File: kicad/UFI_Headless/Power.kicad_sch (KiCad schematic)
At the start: 70 parts, among them J1 USB-C, J16 USB_HDR, J17 PSU_IN, J2 12V DC 5.5/2.1, J3 FDD_PWR, Q1 AO3401A, Q2 2N7002, Q3 AO3401A, Q4 2N7002, U1 USBLC6-2SC6, U12 INA180A1, U13 INA180A1, U19 TPS2116DRL, U2 TPS54202DDC, U24 USBLC6-2SC6, U3 TPS2116DRL, U4 AP7361C-33E

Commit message: KiCad v0.7 rework, stage A11c (owner's device-comparison list M2, order decided 2026-10-24: supply first): drive supplies through two TPS25921A eFuses - Power sheet: U28 (5 V) and U29 (12 V) TI TPS25921ADR (C189199, SOIC-8, JLC stock 681; new project symbol UFI_Headless:TPS25921A with the datasheet pinout 1 GND, 2 SS, 3 ENUV, 4 IN, 5 OUT, 6 FLT, 7 ILIM, 8 OVP) replace the polyfuses F2/F3 and the AO3401A/2N7002 switches Q1-Q4 with their gate network R27/R30/R32; R136/R142 150k (C22807) set the current limit to 1.43-1.7 A (datasheet table for R_ILIM = 150 k), OVP dividers R133/R134 33k/10k = 6.0 V and R138/R139/R140 100k/(10k+1k) = 14.0 V against the 1.39 V threshold (basic parts only, 91k/11k are extended), ENUV from FDD5_EN/FDD12_EN through R135/R141 10k while the existing 100k pull-downs R28/R31 keep both rails off in reset (ENUV threshold 1.39 V, 3.0 V applied), C81 2.2 nF (C1604) and C83 1 nF (C1588) give about 2.5 ms output ramp (datasheet: 1.2 nF = 3 ms at 11 V; measure at bring-up), C80/C82 100 nF at IN, FLT open drain with R137/R143 10k to +3V3 on the new global nets FLT5/FLT12; the shunts R26/R29 with U12/U13 INA180 stay behind the eFuse outputs (FDD5_F/FDD12_F -> shunt -> FDD_5V/FDD_12V, the old FDD5_S/FDD12_S nets are gone); D3 SMAJ15CA -> SMAJ13A (Diodes SMAJ13A-13-F C110519). MCU_Core: PF9 = FLT5, PF10 = FLT12 (no-connects removed). Old v0.2/v0.5 notes replaced by an A11c note. ERC over the whole project 0 errors / 0 warnings (build/erc.rpt). Firmware in the same commit: board.h/board_headless.c PIN_FLT5/PIN_FLT12 as inputs with pull-up (harmless on v0.x where the pins are open), ufi_board.c sample_faults() reads FLT only on board_rev >= 10 and only for a rail that is switched on (FLT is also low while ENUV is low), reports a change once as POWER event 0x83 with ERR LED and leaves the rail on because the eFuse retries by itself, board_status.power bits 2/3 carry the fault state; overcurrent comment updated (eFuse limit instead of polyfuse hold). Protocol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
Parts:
- removed F2, F3: 1.1A hold 24V, Fuse:Fuse_1812_4532Metric, symbol Device:Polyfuse
- removed Q1, Q3: AO3401A, Package_TO_SOT_SMD:SOT-23, symbol Transistor_FET:AO3401A
- removed Q2, Q4: 2N7002, Package_TO_SOT_SMD:SOT-23, symbol Transistor_FET:2N7002
- removed R27: 100k, Resistor_SMD:R_0603_1608Metric, symbol Device:R
- removed R30, R32: 10k, Resistor_SMD:R_0603_1608Metric, symbol Device:R
- added C80, C82: 100nF, Capacitor_SMD:C_0603_1608Metric, symbol Device:C
- added C81: 2.2nF, Capacitor_SMD:C_0603_1608Metric, symbol Device:C
- added C83: 1nF, Capacitor_SMD:C_0603_1608Metric, symbol Device:C
- added R133: 33k, Resistor_SMD:R_0603_1608Metric, symbol Device:R
- added R134, R135, R137, R139, R141, R143: 10k, Resistor_SMD:R_0603_1608Metric, symbol Device:R
- added R136, R142: 150k, Resistor_SMD:R_0603_1608Metric, symbol Device:R
- added R138: 100k, Resistor_SMD:R_0603_1608Metric, symbol Device:R
- added R140: 1k, Resistor_SMD:R_0603_1608Metric, symbol Device:R
- added U28, U29: TPS25921A, Package_SO:SOIC-8_3.9x4.9mm_P1.27mm, symbol UFI_Headless:TPS25921A
- D3: value SMAJ15CA -> SMAJ13A; LCSC C110044 -> C110519; MPN SMAJ15CA -> Diodes SMAJ13A-13-F (13 V standoff, 21.5 V clamp; A11c, was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
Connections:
- net FDD12_S is gone; now on net FDD_12V: R29.2, U13.4 (-)
- net FDD5_S is gone; now on net FDD_5V: R26.2, U12.4 (-)
- net +12V: now also C82.1, R138.1, U29.4 (IN)
- net +3V3: now also R137.1, R143.1
- net +5V: now also C80.1, R133.1, U28.4 (IN)
- net FDD12_EN: now also R141.1
- net FDD12_F: now also U29.5 (OUT)
- net FDD5_EN: now also R135.1
- net FDD5_F: now also U28.5 (OUT)
- net GND: now also C80.2, C81.2, C82.2, C83.2, R134.2, R136.2, R140.2, R142.2, U28.1 (GND), U29.1 (GND)
- new net ENUV12: R141.2, U29.3 (ENUV)
- new net ENUV5: R135.2, U28.3 (ENUV)
- new net FLT12: R143.2, U29.6 (FLT)
- new net FLT5: R137.2, U28.6 (FLT)
- new net ILIM12: R142.1, U29.7 (ILIM)
- new net ILIM5: R136.1, U28.7 (ILIM)
- new net OVP12: R138.2, R139.1, U29.8 (OVP)
- new net OVP12B: R139.2, R140.1
- new net OVP5: R133.2, R134.1, U28.8 (OVP)
- new net SS12: C83.1, U29.2 (SS)
- new net SS5: C81.1, U28.2 (SS)
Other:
- note added: "A11c (24.10.2026): drive supplies through TPS25921A eFuses U28 (5 V) / U29 (12 V) instead of the polyfuses F2/F3 and the AO3401A/2N7002 switches Q1-Q4. R_ILIM 150k -> current limit 1.43-1.7 A (datasheet table), fast trip and auto-retry; OVP divider 33k/10k = 6.0 V, 100k/(10k+1k) = 14.0 V (threshold 1.39 V); ENUV from FDD5_EN/FDD12_EN via 10k, the 100k pull-downs R28/R31 keep both rails off in res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"
- note removed: "v0.2: drive supplies (J3, Amiga J7) via polyfuses; test points TP1-TP4."
- note removed: "v0.5: FDD_5V / FDD_12V: polyfuse -> 0.1R shunt (INA180A1 -> I_FDD5/I_FDD12, 2 V/A) -> AO3401A high-side switch (FDD5_EN/FDD12_EN high = on, 100k pull-downs = off in reset) -> TVS. 12V gate divider 10k/10k keeps Vgs at -6 V (AO3401A max +-12 V)."

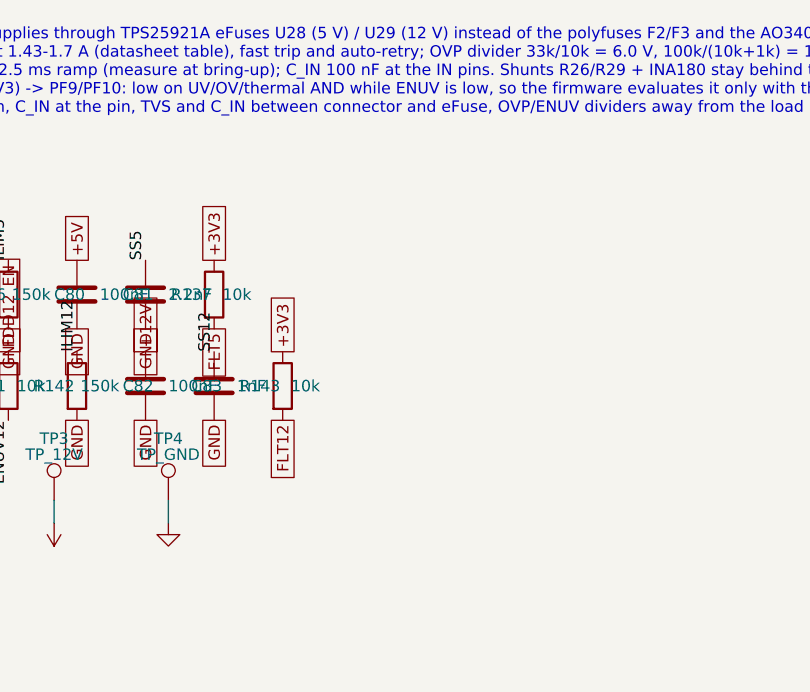
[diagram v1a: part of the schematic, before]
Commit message: KiCad v0.7 rework, stage A11d part 1 (owner's device-comparison list M5, S1-S4, S6; pins per docs/Timer_Zuteilung.md): sync sensor, J6 pin 2/4/33, rail voltage sense - Apple_Port: J19 pin 3 leaves the INDEX bus and becomes SYNC_5V with R165 10k to +3V3 and D30 PESD3V3L1BA, the new third Schmitt inverter U26 74LVC14AD (C133541, single-unit project symbol UFI_Headless:74LVC14_1U) turns it into SYNC -> PC6 (TIM8_CH1, AF3), also reads J6 pin 2 (FD_DENSITY) and pin 4 (FD_PIN4) back as FDD_PIN2_IN -> PD14 / FDD_PIN4_IN -> PD15 and reserves input 9 for the Mac !CSTOUT line of K1 (no-connect until A11d part 2), unused inputs on GND, C86 100 nF. FDD_Connectors: J6 pin 4 gets its own open-drain output Q12 BSS138DW (C154900, channel 1, gate FDD_PIN4 = PF14 with R158 100k, termination R159 1k to FDD_5V); J6 pin 33 moves from a fixed GND to the solder jumper JP7 (bridged to GND by default) whose third pad carries FLIPPY = PB5 through R156 2.2k with R157 2.2k to GND (2.2k instead of the planned 2.4k because 2.2k C4190 is already in the BOM). Power: R160/R161 10k/10k (FDD_5V / 2 -> V_FDD5 = PC4, ADC1 INP4) and R162/R163 33k/10k (FDD_12V / 4.3 -> V_FDD12 = PC5, ADC1 INP8). MCU_Core: no-connects on PC6, PD14, PD15, PF14, PB5, PC4, PC5, PB1 replaced by the global labels; PB0 (MAC_SEL) and PA8 (MAC_PWM) stay no-connect until the Mac header comes in part 2, PB1 = MAC_CSTOUT is already wired to U26. ERC over the whole project 0 errors / 0 warnings (build/erc.rpt). Firmware in the same commit: board.h/board_headless.c define PIN_SYNC, PIN_FDD_PIN2_IN, PIN_FDD_PIN4_IN, PIN_FDD_PIN4, PIN_FDD_PIN33, PIN_MAC_SEL, PIN_MAC_PWM, PIN_MAC_CSTOUT and ADC_CH_V_FDD5/V_FDD12 and initialise them as inputs or released (low) outputs; the TIM8 capture of SYNC, the rail-voltage limits (4.5 V / 10.8 V) and the protocol access follow in stage A10 (protocol doc: one hunk in the INDEX_SIM bullet - the sync sensor no longer drives the INDEX bus on v1.0, apple_sync has no effect there until A10). ARM build 0 wa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
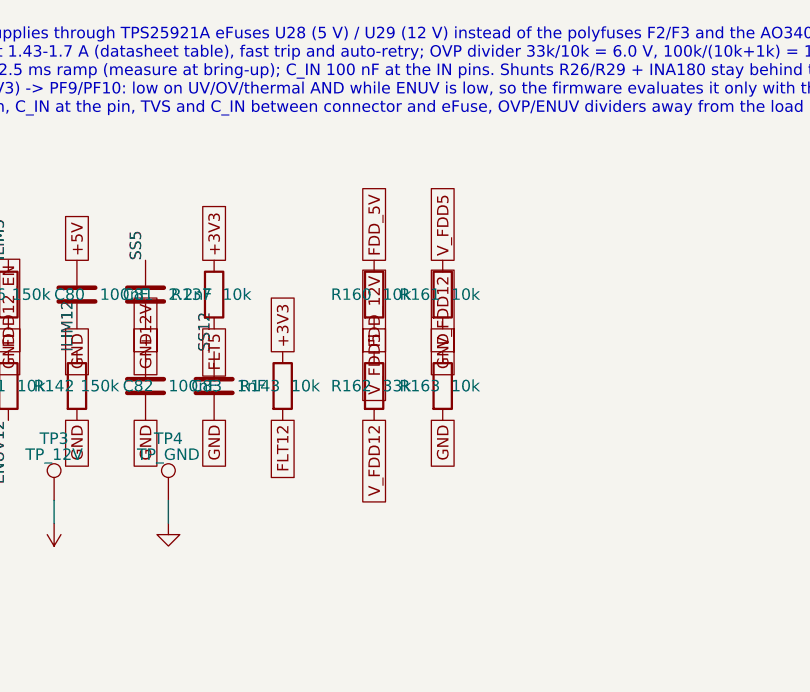
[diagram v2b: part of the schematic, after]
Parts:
- added R160, R161, R163: 10k, Resistor_SMD:R_0603_1608Metric, symbol Device:R
- added R162: 33k, Resistor_SMD:R_0603_1608Metric, symbol Device:R
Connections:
- net FDD_12V: now also R162.1
- net FDD_5V: now also R160.1
- net GND: now also R161.2, R163.2
- new net V_FDD12: R162.2, R163.1
- new net V_FDD5: R160.2, R161.1

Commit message: KiCad v0.7 rework, stage A11d part 2 (owner's list S5, S7, K1; owner decisions 2026-10-24: no D-sub on the board, pins 9/20 through solder jumpers default open, PWM line always on a Schmitt input, no fuse on the -12 V): Apple_Port: new Mac 3.5" port J23 (2x10 IDC, UFI_Headless:IDC-Header_2x10_P2.54mm_Vertical_UFI, C2977593) in the Apple internal 20-pin floppy pinout taken from the tashnotes connector document - 1/3/5/7 GND, 2/4/6/8 CA0/CA1/CA2/LSTRB on the Disk II phase nets AP_PH0-3, 10 !WRREQ (AP_WRREQ, gated by LOCK since A11a), 12 SEL = MAC_SEL_5V, 14 !ENBL = AP_EN2 (J15 removed), 16 RD = AP_RDDATA, 18 WR = AP_WRDATA, 11 FDD_5V, 13/15/17/19 FDD_12V, 9 = AP_M12V_J6 only through JP6 (open; 800K/FDHD drives output !EJECT there), 20 = CSTOUT_5V with R166 10k to FDD_5V, fed by the PWM driver only through JP5 (open; 800K/FDHD output !CSTOUT there) and always read back through U26 pin 9 -> MAC_CSTOUT = PB1; U27 SN74AHCT244PWR (C484743, FDD_5V, C87 100 nF) shifts MAC_SEL (PB0) and MAC_PWM (PA8, TIM1_CH1) to 5 V, unused inputs on GND and unused outputs no-connect; D31 ESDA6V1-5SC6 (C6650) on SEL and pin 20. S5: JP8 (bridged) between the ICL7662 output AP_M12V and J14 pin 9 (AP_M12V_J), no fuse - the pump limits to about 20 mA; U18 stays the ICL7662. Power: S7 USB shield J1 SH leaves GND and goes through R164 1M (C22935) parallel C85 4.7 nF (C53987) to GND (net USB_SHIELD). MCU_Core: PB0 = MAC_SEL and PA8 = MAC_PWM wired (no-connects removed). Notes on the Apple sheet. ERC over the whole project 0 errors / 0 warnings (build/erc.rpt). No firmware change in this part (the pins were defined and initialised released in part 1; the Mac drive driver SEL/PWM/CSTOUT and the 800K/FDHD GCR path are a firmware stage after A10), therefore no protocol change. PLAN.md (A11d complete, A11 done except the layout), kicad README (A11d-2 row). PCB follows in B3 (J23 placement with cable exit towards the enclosure socket).
Claude-Session: https://claude.ai/code/session_014MdzrcyXuayppPHbfEjU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
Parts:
- added C85: 4.7nF, Capacitor_SMD:C_0603_1608Metric, symbol Device:C
- added R164: 1M, Resistor_SMD:R_0603_1608Metric, symbol Device:R
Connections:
- net GND: now also C85.2, R164.2; no longer J1.SH (SHIELD)
- new net USB_SHIELD: C85.1, J1.SH (SHIELD), R164.1
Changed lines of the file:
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@@
 	(wire
 		(pts
-			(xy 33.02 111.76) (xy 33.02 114.3)
-		)
-		(stroke
-			(width 0)
-			(type default)
-		)
-	)
-	(wire
-		(pts
 			(xy 78.74 72.39) (xy 78.74 69.85)
 		)
@@
 	)
 	(symbol
-		(lib_id "power:GND")
-		(at 33.02 114.3 0)
-		(unit 1)
-		(exclude_from_sim no)
-		(in_bom no)
-		(on_board yes)
-		(dnp no)
-		(property "Reference" "#PWR003"
-			(at 33.02 120.65 0)
-			(effects
-				(font
-					(size 1.27 1.27)
-				)
-				(hide yes)
-			)
-		)
-		(property "Value" "GND"
-			(at 33.02 118.11 0)
-			(effects
-				(font
-					(size 1.27 1.27)
-				)
-				(hide yes)
-			)
-		)
-		(property "Footprint" ""
-			(at 33.02 114.3 0)
-			(effects
-				(font
-					(size 1.27 1.27)
-				)
-				(hide yes)
-			)
-		)
-		(property "Datasheet" ""
-			(at 33.02 114.3 0)
-			(effects
-				(font
-					(size 1.27 1.27)
-				)
-				(hide yes)
-			)
-		)
-		(pin "1"
-		)
-		(instances
-			(project "UFI_Headless"
-				(path "/dc1b800d-cedf-5627-97f0-e6992ff33669/fbe2b8a8-7a93-5a0f-a2a9-1800b176cb77"
-					(reference "#PWR003")
-					(unit 1)
-				)
-			)
-		)
-	)
-	(symbol
 		(lib_id "Connector:USB_C_Receptacle_USB2.0_16P")
 		(at 40.64 88.9 0)
@@
 			)
 		)
-    (property "LCSC" "C25804" (at 360.68 215.9 0)
-      (effects (font (size 1.27 1.27)) (hide yes))
-    )
+		(property "LCSC" "C25804"
+			(at 360.68 215.9 0)
+			(effects
+				(font
+					(size 1.27 1.27)
+				)
+				(hide yes)
+			)
+		)
 		(pin "1"
 		)
@@
 			)
 		)
-    (property "LCSC" "C25804" (at 368.3 215.9 0)
-      (effects (font (size 1.27 1.27)) (hide yes))
-    )
+		(property "LCSC" "C25804"
+			(at 368.3 215.9 0)
+			(effects
+				(font
+					(size 1.27 1.27)
+				)
+				(hide yes)
+			)
+		)
 		(pin "1"
 		)
@@
 			)
 		)
-    (property "LCSC" "C4216" (at 360.68 226.06 0)
-      (effects (font (size 1.27 1.27)) (hide yes))
-    )
+		(property "LCSC" "C4216"
+			(at 360.68 226.06 0)
+			(effects
+				(font
+					(size 1.27 1.27)
+				)
+				(hide yes)
+			)
+		)
 		(pin "1"
 		)
@@
 			)
 		)
-    (property "LCSC" "C25804" (at 368.3 226.06 0)
-      (effects (font (size 1.27 1.27)) (hide yes))
-    )
+		(property "LCSC" "C25804"
+			(at 368.3 226.06 0)
+			(effects
+				(font
+					(size 1.27 1.27)
+				)
+				(hide yes)
+			)
+		)
 		(pin "1"
 		)
@@
 		)
 	)
+	(symbol
+		(lib_id "Device:R")
+		(at 25.4 124.46 0)
+		(unit 1)
+		(exclude_from_sim no)
+		(in_bom yes)
+		(on_board yes)
+		(dnp no)
+		(property "Reference" "R164"
+			(at 22.86 124.46 0)
+			(show_name no)
+			(do_not_autoplace no)
+			(effects
+				(font
+					(size 1.27 1.27)
+				)
+			)
+		)
+		(property "Value" "1M"
+			(at 27.94 124.46 0)
+			(show_name no)
+			(do_not_autoplace no)
+			(effects
+				(font
+					(size 1.27 1.27)
+				)
+			)
+		)
+		(property "Footprint" "Resistor_SMD:R_0603_1608Metric"
+			(at 23.622 124.46 90)
+			(hide yes)
+			(show_name no)
+			(do_not_autoplace no)
+			(effects
+				(font
+					(size 1.27 1.27)
+				)
+			)
+		)
+		(property "Datasheet" ""
+			(at 25.4 124.46 0)
+			(hide yes)
+			(show_name no)
+			(do_not_autoplace no)
+			(effects
+				(font
+					(size 1.27 1.27)
+				)
+			)
+		)
+		(property "Description" "Resistor"
+			(at 25.4 124.46 0)
+			(hide yes)
+			(show_name no)
+			(do_not_autoplace no)
+			(effects
+				(font
+					(size 1.27 1.27)
+				)
+			)
+		)
+    (property "LCSC" "C22935" (at 25.4 124.46 0)
+      (effects (font (size 1.27 1.27)) (hide yes))
+    )
+    (property "MPN" "1M (USB shield to GND, A11d S7)" (at 25.4 124.46 0)
+      (effects (font (size 1.27 1.27)) (hide yes))
+    )
+		(pin "1"
+		)
+		(pin "2"
+		)
+		(instances
+			(project "UFI_Headless"
+				(path "/dc1b800d-cedf-5627-97f0-e6992ff33669/fbe2b8a8-7a93-5a0f-a2a9-1800b176cb77"
+					(reference "R164")
+					(unit 1)
+				)
+			)
+		)
+	)
+	(symbol
+		(lib_id "Device:C")
+		(at 33.02 124.46 0)
+		(unit 1)
+		(exclude_from_sim no)
+		(in_bom yes)
+		(on_board yes)
+		(dnp no)
+		(property "Reference" "C85"
+			(at 30.48 124.46 0)
+			(show_name no)
+			(do_not_autoplace no)
+			(effects
+				(font
+					(size 1.27 1.27)
+				)
+				(justify left)
+			)
+		)
+		(property "Value" "4.7nF"
+			(at 35.56 124.46 0)
+			(show_name no)
+			(do_not_autoplace no)
+			(effects
+				(font
+					(size 1.27 1.27)
+				)
+				(justify left)
+			)
+		)
+		(property "Footprint" "Capacitor_SMD:C_0603_1608Metric"
+			(at 33.985 120.65 0)
+			(hide yes)
+			(show_name no)
+			(do_not_autoplace no)
+			(effects
+				(font
+					(size 1.27 1.27)
+				)
+			)
+		)
+		(property "Datasheet" ""
+			(at 33.02 124.46 0)
+			(hide yes)
+			(show_name no)
+			(do_not_autoplace no)
+			(effects
+				(font
+					(size 1.27 1.27)
+				)
+			)
+		)
+		(property "Description" "Unpolarized capacitor"
+			(at 33.02 124.46 0)
+			(hide yes)
+			(show_name no)
+			(do_not_autoplace no)
+			(effects
+				(font
+					(size 1.27 1.27)
+				)
+			)
+		)
+    (property "LCSC" "C53987" (at 33.02 124.46 0)
+      (effects (font (size 1.27 1.27)) (hide yes))
+    )
+    (property "MPN" "4.7nF 50V X7R (USB shield to GND, A11d S7)" (at 33.02 124.46 0)
+      (effects (font (size 1.27 1.27)) (hide yes))
+    )
+		(pin "1"
+		)
+		(pin "2"
+		)
+		(instances
+			(project "UFI_Headless"
+				(path "/dc1b800d-cedf-5627-97f0-e6992ff33669/fbe2b8a8-7a93-5a0f-a2a9-1800b176cb77"
+					(reference "C85")
+					(unit 1)
+				)
+			)
+		)
+	)
+	(global_label "GND"
+		(at 25.4 128.26999999999998 270)
+		(effects
+			(font
+				(size 1.27 1.27)
+			)
+			(justify right)
+		)
+	)
+	(global_label "GND"
+		(at 33.02 128.26999999999998 270)
+		(effects
+			(font
+				(size 1.27 1.27)
+			)
+			(justify right)
+		)
+	)
+	(label "USB_SHIELD"
+		(at 33.02 111.76 270)
+		(effects
+			(font
+				(size 1.27 1.27)
+			)
+			(justify right bottom)
+		)
+	)
+	(wire
+		(pts
+			(xy 25.4 120.64999999999999) (xy 33.02 111.76)
+		)
+		(stroke
+			(width 0)
+			(type default)
+		)
+	)
+	(wire
+		(pts
+			(xy 33.02 120.64999999999999) (xy 33.02 111.76)
+		)
+		(stroke
+			(width 0)
+			(type default)
+		)
+	)

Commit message: KiCad v0.7 rework, stage C part 1 (BOM completion before the release, review note H12): every BOM row now carries an LCSC number, checked against the JLCPCB SMT catalogue on 2026-10-25 (stock in brackets). LAN sheet: U23 W5500 C32843 (9019), J22 HR911105A C12074 (72229, THT), Y2 25 MHz 12 pF +-10 ppm YXC X322525MOB4SI C9006 (basic; load capacitance 12 pF verified on the LCSC parameter page, fits the 18 pF C59/C60), C59/C60 18 pF C0G Yageo CC0603JRNPO9BN180 C107040, C61/C74 10 nF FH 0603B103K500NT C57112 (basic), C71 22 nF Samsung CL10B223KB8NNNC C21122 (basic), C72/C73 6.8 nF FH 0603B682K500NT C1631 (basic), C62 4.7 uF C1779, C63/C69 10 uF C15850, C64-C68/C70 100 nF C14663, FB2 C1002, R109 1M C22935, R111 12.4k 1 % C22865, R112/R113 49.9R 1 % C23185 (basic), R114 10R 1 % C22859 (basic), R115/R116 82R 1 % C23255, R117/R118 330R C23138, R119-R124 10k C25804. Other sheets: R75-R99/R105/R128 1k C21190, R74/R107/R108 10k C25804, R101-R104/R130 470R C23179, R106/R131 100k C25803, C58 100 nF C14663 (value text 100n -> 100nF so it groups with the other 100 nF), D18-D26/D28/D29 PESD3V3L1BA C51450 (48710) like D32-D34, Q5 2N7002 C8545 (basic), U22 TS5A3166DBVR C353035 (10678), J2 DC-005 2.0 C16214 (92305; same pin pattern as the KiCad BarrelJack_Horizontal footprint, placement to be checked in the JLC viewer), J7 2x12 IDC ZHOURI DC3-2.54-24PAS C5144580 (stock 81 - hand soldering stays the recommendation in docs/Bestellung_JLC.md), J12 2x8 IDC DC3-2.54-16PAS C2977594 (4335), J16 2x5 pin header XFCN PZ254V-12-10P C492422 (105667), J21 2x10 pin header PZ254V-12-20P C492427 (63622). Solder jumpers JP5-JP8 are excluded from the BOM (in_bom no) like JP1/JP3 - bare copper, nothing to place. Stock of the review's watch list: U9 SN74LS07DR C371970 4776, D31 ESDA6V1-5SC6 C6650 3010, L1 SRN6045TA-150M C1330797 1866. BOM export (kicad-cli sch export bom, grouped by value/footprint/LCSC): 99 rows, 0 without LCSC, 0 DNP. ERC over the whole project 0 errors / 0 warnings (build/erc.rpt). No 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
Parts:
- J16: LCSC (none) -> C492422
- J2: LCSC (none) -> C16214
- R74: LCSC (none) -> C25804
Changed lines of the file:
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@@
 			)
 		)
+		(property "LCSC" "C16214"
+			(at 41.91 171.196 0)
+			(effects
+				(font
+					(size 1.27 1.27)
+				)
+				(hide yes)
+			)
+		)
 		(property "Footprint" "Connector_BarrelJack:BarrelJack_Horizontal"
 			(at 41.91 171.196 0)
@@
 			)
 		)
+		(property "LCSC" "C492422"
+			(at 40.64 248.92 0)
+			(effects
+				(font
+					(size 1.27 1.27)
+				)
+				(hide yes)
+			)
+		)
 		(property "Footprint" "Connector_PinHeader_2.54mm:PinHeader_2x05_P2.54mm_Vertical"
 			(at 40.64 248.92 0)
@@
 			)
 		)
+		(property "LCSC" "C25804"
+			(at 201.422 259.08 90)
+			(effects
+				(font
+					(size 1.27 1.27)
+				)
+				(hide yes)
+			)
+		)
